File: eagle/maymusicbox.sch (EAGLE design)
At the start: 39 parts, among them CN1 BATT, Q1 IRF9530

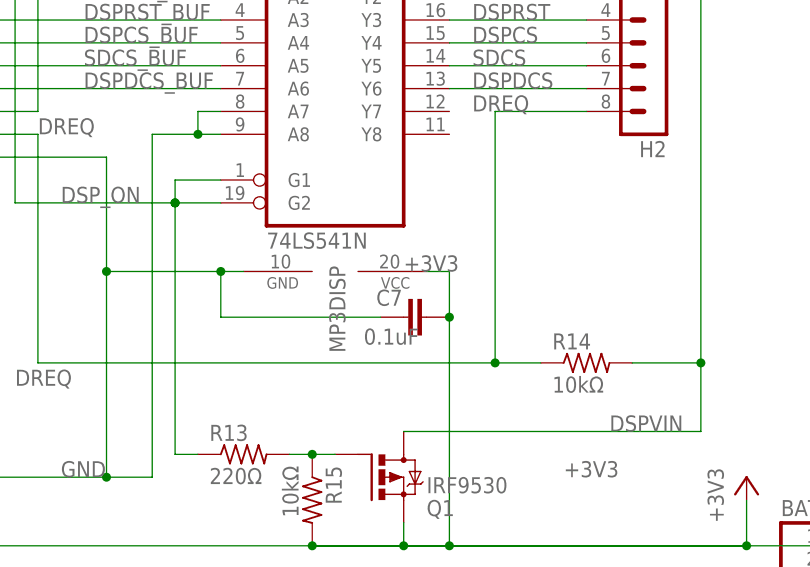
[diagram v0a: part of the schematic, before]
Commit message: Fix Schematic + Part to have 0 error issues
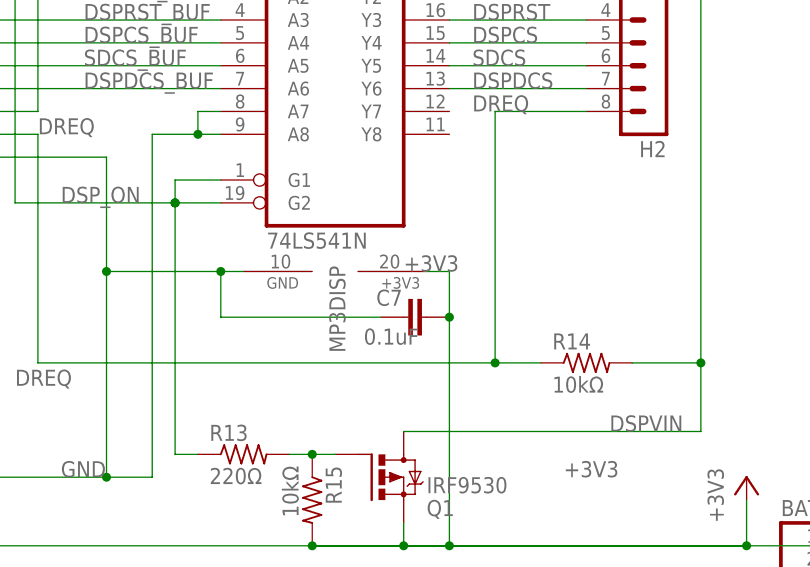
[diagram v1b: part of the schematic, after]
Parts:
- MP3DIS: device 74xx-us:74LS541N -> May Music Box Parts:74LS541N
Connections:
- net +3V3: now also MP3DISP.+3V3; no longer MP3DISP.VCC
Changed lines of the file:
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@@
 </classes>
 <parts>
-<part name="MP3DIS" library="74xx-us" deviceset="74*541" device="N" technology="LS"/>
+<part name="MP3DIS" library="May Music Box Parts" deviceset="74*541" device="N" technology="LS"/>
 <part name="C1" library="rcl" deviceset="C-EU" device="025-025X050" value="1uF"/>
 <part name="R1" library="resistor" deviceset="R-US_" device="0207/2V" value="10k"/>
@@
 <junction x="66.04" y="2.54"/>
 <label x="15.24" y="2.54" size="1.778" layer="95"/>
-<pinref part="MP3DIS" gate="P" pin="VCC"/>
+<pinref part="MP3DIS" gate="P" pin="+3V3"/>
 <wire x1="78.74" y1="33.02" x2="81.28" y2="33.02" width="0.1524" layer="91"/>
 <wire x1="81.28" y1="33.02" x2="81.28" y2="27.94" width="0.1524" layer="91"/>
@@
 </sheet>
 </sheets>
-<errors>
-</errors>
 </schematic>
 </drawing>
